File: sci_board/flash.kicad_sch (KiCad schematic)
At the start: 4 parts, among them U30 MT29F4G01ABAFDWB-IT:F TR

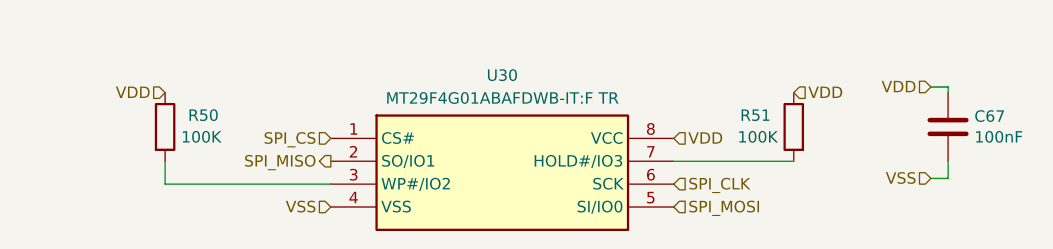
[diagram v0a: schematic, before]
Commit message: add SPI CS and MISO pullups and terminations, remove WD from SCI
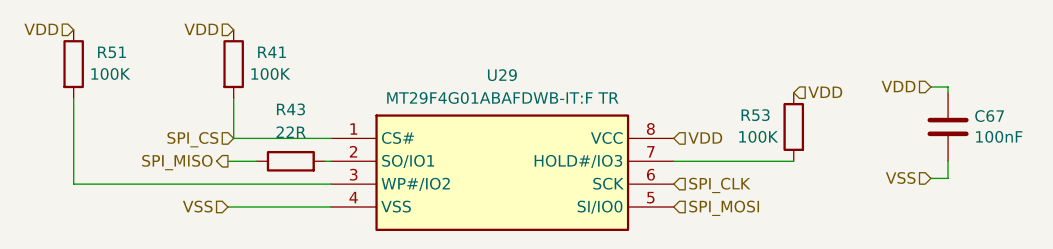
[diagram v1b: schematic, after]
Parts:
- added R41: 100K, Resistor_SMD:R_0402_1005Metric_Pad0.72x0.64mm_HandSolder, symbol Device:R
- added R43: 22R, Resistor_SMD:R_0402_1005Metric_Pad0.72x0.64mm_HandSolder, symbol Device:R
- renumbered R50 to R51, R51 to R53, U30 to U29
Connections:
- net SPI_CS: now also R41.2
- net SPI_MISO: now also R43.1; no longer U29.2 (SO/IO1)
- net VDD: now also R41.1
- new net: R43.2, U29.2 (SO/IO1)
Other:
- moved on the sheet: R51

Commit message: tweaking SCI and AUX for production, using common sheets as much as possible
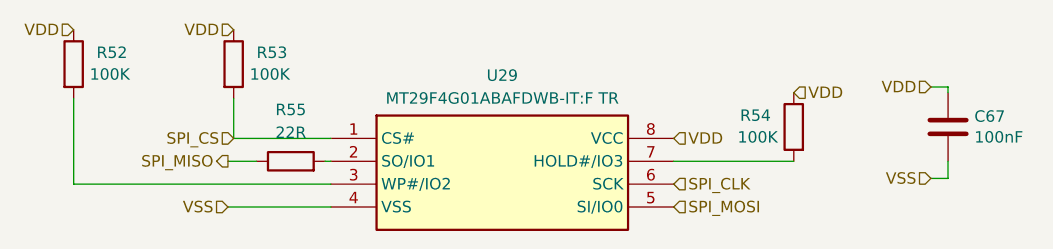
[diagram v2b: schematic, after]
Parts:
- renumbered R51 to R52, R41 to R53, R53 to R54, R43 to R55
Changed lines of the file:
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@@
 		(on_board yes)
 		(dnp no)
-		(property "Reference" "R41"
+		(property "Reference" "R53"
 			(at 64.135 63.5 0)
 			(effects
@@
 			(project "sci_board"
 				(path "/b4b2c88d-f6cd-4e60-862d-e21f68728580/1e53aba3-dd28-4d46-80f1-455dd7d8f930"
-					(reference "R52")
+					(reference "R53")
 					(unit 1)
 				)
@@
 		(on_board yes)
 		(dnp no)
-		(property "Reference" "R51"
+		(property "Reference" "R52"
 			(at 46.355 63.5 0)
 			(effects
@@
 			(project "sci_board"
 				(path "/b4b2c88d-f6cd-4e60-862d-e21f68728580/1e53aba3-dd28-4d46-80f1-455dd7d8f930"
-					(reference "R51")
+					(reference "R52")
 					(unit 1)
 				)
@@
 		(on_board yes)
 		(dnp no)
-		(property "Reference" "R53"
+		(property "Reference" "R54"
 			(at 121.285 70.485 0)
 			(effects
@@
 			(project "sci_board"
 				(path "/b4b2c88d-f6cd-4e60-862d-e21f68728580/1e53aba3-dd28-4d46-80f1-455dd7d8f930"
-					(reference "R53")
+					(reference "R54")
 					(unit 1)
 				)
@@
 		(dnp no)
 		(fields_autoplaced yes)
-		(property "Reference" "R43"
+		(property "Reference" "R55"
 			(at 67.945 69.85 90)
 			(effects
@@
 			(project ""
 				(path "/b4b2c88d-f6cd-4e60-862d-e21f68728580/1e53aba3-dd28-4d46-80f1-455dd7d8f930"
-					(reference "R54")
-					(unit 1)
-				)
+					(reference "R55")
+					(unit 1)
+				)

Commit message: clenup BOM for SCI and AUX
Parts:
- R55: Manufacturer (none) -> YAGEO; Part Number (none) -> RC0402FR-0722RL; Tolerance (none) -> 1
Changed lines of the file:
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@@
 			)
 		)
-		(property "Datasheet" "~"
+		(property "Datasheet" "https://www.yageo.com/upload/media/product/app/datasheet/rchip/pyu-rt_1-to-0.01_rohs_l.pdf"
 			(at 67.945 75.565 0)
 			(effects
@@
 			(at 67.945 75.565 0)
 			(effects
+				(font
+					(size 1.27 1.27)
+				)
+				(hide yes)
+			)
+		)
+		(property "Manufacturer" "YAGEO"
+			(at 67.945 75.565 0)
+			(effects
+				(font
+					(size 1.27 1.27)
+				)
+				(hide yes)
+			)
+		)
+		(property "Part Number" "RC0402FR-0722RL"
+			(at 67.945 75.565 0)
+			(effects
+				(font
+					(size 1.27 1.27)
+				)
+				(hide yes)
+			)
+		)
+		(property "Tolerance" "1"
+			(at 67.945 75.565 0)
+			(effects

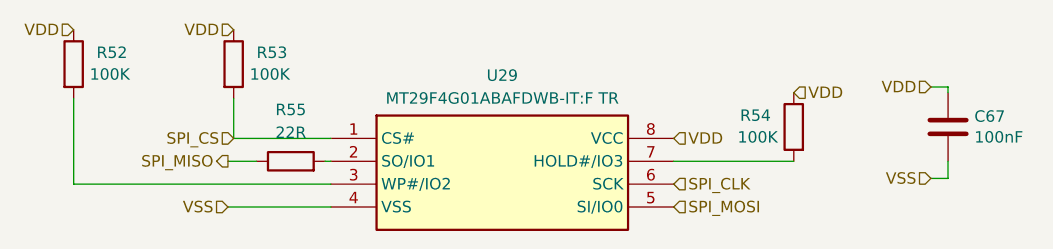
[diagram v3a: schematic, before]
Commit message: cleaning up bom: remove main camera port since it has not pullups and capacitors, correcting some errors in camera switch
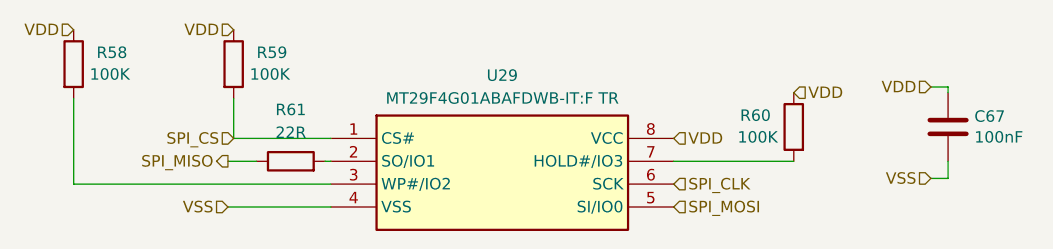
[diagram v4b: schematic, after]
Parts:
- renumbered R52 to R58, R53 to R59, R54 to R60, R55 to R61
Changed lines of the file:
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@@
 		(on_board yes)
 		(dnp no)
-		(property "Reference" "R53"
+		(property "Reference" "R59"
 			(at 64.135 63.5 0)
 			(effects
@@
 			(project "sci_board"
 				(path "/b4b2c88d-f6cd-4e60-862d-e21f68728580/1e53aba3-dd28-4d46-80f1-455dd7d8f930"
-					(reference "R53")
+					(reference "R59")
 					(unit 1)
 				)
 				(path "/b4b2c88d-f6cd-4e60-862d-e21f68728580/f6b358f0-c3e5-4f27-97bc-30bc2986accd"
-					(reference "R41")
+					(reference "R47")
 					(unit 1)
 				)
@@
 		(on_board yes)
 		(dnp no)
-		(property "Reference" "R52"
+		(property "Reference" "R58"
 			(at 46.355 63.5 0)
 			(effects
@@
 			(project "sci_board"
 				(path "/b4b2c88d-f6cd-4e60-862d-e21f68728580/1e53aba3-dd28-4d46-80f1-455dd7d8f930"
-					(reference "R52")
+					(reference "R58")
 					(unit 1)
 				)
 				(path "/b4b2c88d-f6cd-4e60-862d-e21f68728580/f6b358f0-c3e5-4f27-97bc-30bc2986accd"
-					(reference "R40")
+					(reference "R46")
 					(unit 1)
 				)
@@
 		(on_board yes)
 		(dnp no)
-		(property "Reference" "R54"
+		(property "Reference" "R60"
 			(at 121.285 70.485 0)
 			(effects
@@
 			(project "sci_board"
 				(path "/b4b2c88d-f6cd-4e60-862d-e21f68728580/1e53aba3-dd28-4d46-80f1-455dd7d8f930"
-					(reference "R54")
+					(reference "R60")
 					(unit 1)
 				)
 				(path "/b4b2c88d-f6cd-4e60-862d-e21f68728580/f6b358f0-c3e5-4f27-97bc-30bc2986accd"
-					(reference "R42")
+					(reference "R48")
 					(unit 1)
 				)
@@
 		(dnp no)
 		(fields_autoplaced yes)
-		(property "Reference" "R55"
+		(property "Reference" "R61"
 			(at 67.945 69.85 90)
 			(effects
@@
 			(project ""
 				(path "/b4b2c88d-f6cd-4e60-862d-e21f68728580/1e53aba3-dd28-4d46-80f1-455dd7d8f930"
-					(reference "R55")
+					(reference "R61")
 					(unit 1)
 				)
 				(path "/b4b2c88d-f6cd-4e60-862d-e21f68728580/f6b358f0-c3e5-4f27-97bc-30bc2986accd"
-					(reference "R43")
-					(unit 1)
-				)
+					(reference "R49")
+					(unit 1)
+				)

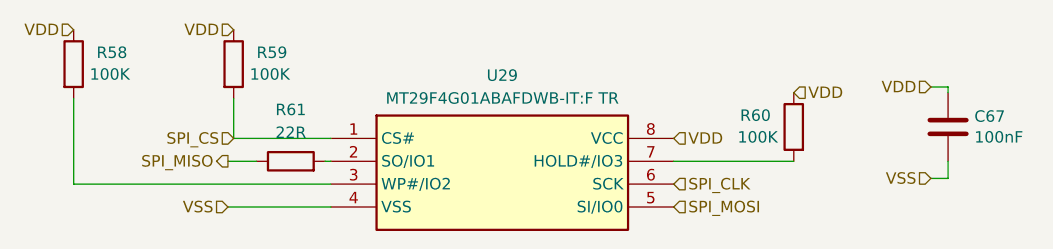
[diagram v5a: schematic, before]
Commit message: local switches and monitors for SCI and RF
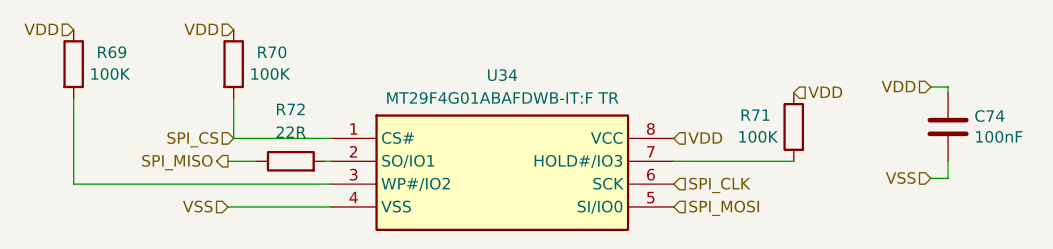
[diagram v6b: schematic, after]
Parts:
- renumbered C67 to C74, R58 to R69, R59 to R70, R60 to R71, R61 to R72, U29 to U34
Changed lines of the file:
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@@
 		(on_board yes)
 		(dnp no)
-		(property "Reference" "C67"
+		(property "Reference" "C74"
 			(at 143.891 70.5866 0)
 			(effects
@@
 			(project "sci_board"
 				(path "/b4b2c88d-f6cd-4e60-862d-e21f68728580/1e53aba3-dd28-4d46-80f1-455dd7d8f930"
-					(reference "C67")
+					(reference "C74")
 					(unit 1)
 				)
 				(path "/b4b2c88d-f6cd-4e60-862d-e21f68728580/f6b358f0-c3e5-4f27-97bc-30bc2986accd"
-					(reference "C59")
+					(reference "C62")
 					(unit 1)
 				)
@@
 		(dnp no)
 		(fields_autoplaced yes)
-		(property "Reference" "U29"
+		(property "Reference" "U34"
 			(at 91.44 66.04 0)
 			(effects
@@
 			(project "sci_board"
 				(path "/b4b2c88d-f6cd-4e60-862d-e21f68728580/1e53aba3-dd28-4d46-80f1-455dd7d8f930"
-					(reference "U29")
+					(reference "U34")
 					(unit 1)
 				)
 				(path "/b4b2c88d-f6cd-4e60-862d-e21f68728580/f6b358f0-c3e5-4f27-97bc-30bc2986accd"
-					(reference "U26")
+					(reference "U28")
 					(unit 1)
 				)
@@
 		(on_board yes)
 		(dnp no)
-		(property "Reference" "R59"
+		(property "Reference" "R70"
 			(at 64.135 63.5 0)
 			(effects
@@
 			(project "sci_board"
 				(path "/b4b2c88d-f6cd-4e60-862d-e21f68728580/1e53aba3-dd28-4d46-80f1-455dd7d8f930"
-					(reference "R59")
+					(reference "R70")
 					(unit 1)
 				)
 				(path "/b4b2c88d-f6cd-4e60-862d-e21f68728580/f6b358f0-c3e5-4f27-97bc-30bc2986accd"
-					(reference "R47")
+					(reference "R52")
 					(unit 1)
 				)
@@
 		(on_board yes)
 		(dnp no)
-		(property "Reference" "R58"
+		(property "Reference" "R69"
 			(at 46.355 63.5 0)
 			(effects
@@
 			(project "sci_board"
 				(path "/b4b2c88d-f6cd-4e60-862d-e21f68728580/1e53aba3-dd28-4d46-80f1-455dd7d8f930"
-					(reference "R58")
+					(reference "R69")
 					(unit 1)
 				)
 				(path "/b4b2c88d-f6cd-4e60-862d-e21f68728580/f6b358f0-c3e5-4f27-97bc-30bc2986accd"
-					(reference "R46")
+					(reference "R51")
 					(unit 1)
 				)
@@
 		(on_board yes)
 		(dnp no)
-		(property "Reference" "R60"
+		(property "Reference" "R71"
 			(at 121.285 70.485 0)
 			(effects
@@
 			(project "sci_board"
 				(path "/b4b2c88d-f6cd-4e60-862d-e21f68728580/1e53aba3-dd28-4d46-80f1-455dd7d8f930"
-					(reference "R60")
+					(reference "R71")
 					(unit 1)
 				)
 				(path "/b4b2c88d-f6cd-4e60-862d-e21f68728580/f6b358f0-c3e5-4f27-97bc-30bc2986accd"
-					(reference "R48")
+					(reference "R53")
 					(unit 1)
 				)
@@
 		(dnp no)
 		(fields_autoplaced yes)
-		(property "Reference" "R61"
+		(property "Reference" "R72"
 			(at 67.945 69.85 90)
 			(effects
@@
 			(project ""
 				(path "/b4b2c88d-f6cd-4e60-862d-e21f68728580/1e53aba3-dd28-4d46-80f1-455dd7d8f930"
-					(reference "R61")
+					(reference "R72")
 					(unit 1)
 				)
 				(path "/b4b2c88d-f6cd-4e60-862d-e21f68728580/f6b358f0-c3e5-4f27-97bc-30bc2986accd"
-					(reference "R49")
-					(unit 1)
-				)
+					(reference "R54")
+					(unit 1)
+				)
